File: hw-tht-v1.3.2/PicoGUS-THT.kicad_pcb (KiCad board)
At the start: 2 copper layers, 103.7 x 99.8 mm, 88 parts, among them J1 IRQDMA_JP, J11 USB-A, J3 Bus_ISA_8bit, J5 SJ1-3535NG, J6 UART_TX, J7 USB power jumper, J8 SJ1-3535NG-GR, J9 Waveblaster, U1 Pico, U10 74AHCT126, U11 NE5532, U12 USBLC6-2SC6, U2 74AHC244, U3 SN74CB3T3257, U4 SN74CB3T3257, U5 74AHC14, U6 74AHC00, U7 74AHC00, U8 APS6404L-3SQR-SN, U9 PCM5100A

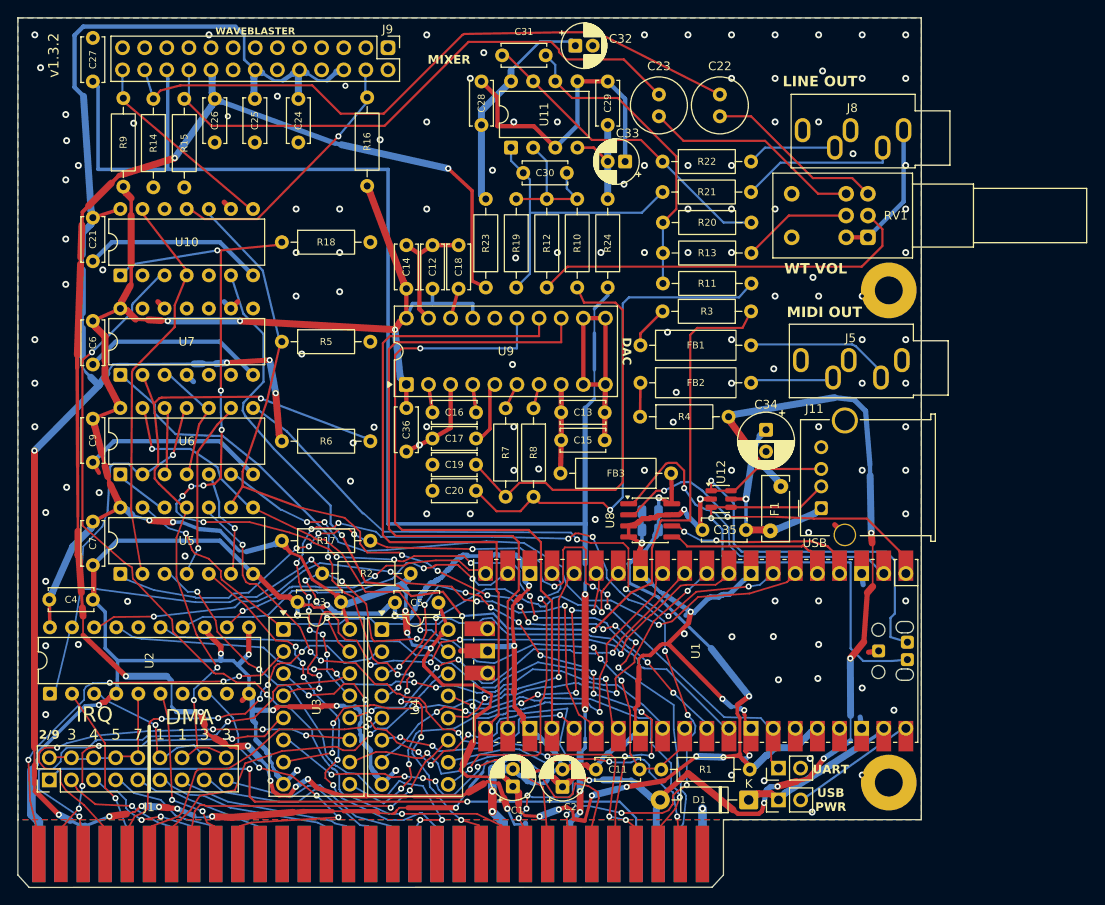
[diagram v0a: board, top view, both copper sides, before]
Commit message: THT v1.3.2: adopt the 102 mm placement (unrouted) with 3D models
The board now holds the new hand placement on a 102.0 mm outline in place
of the routed 103.7 mm layout (that one stays in 8dbb6c6). It has no
tracks or vias yet and has to be routed again.

- Logic column in line with U2 with the decoupling discs between the
  chips, R18/R5/R6/R17 vertical, DAC group 15 mm left, FB3 vertical,
  copper logo along the top edge over LINE OUT, several labels moved.
- C8/C10 back to the v1.3.1 Murata through-hole discs, in a row above
  U8 (schematic fields, BOM and DigiKey upload files updated).
- Back princess artwork removed (to be UV printed); back texts kept.
- Bracket end trimmed 1.84 mm (JLCPCB prices <= 102 mm lower). H1/H2
  1.70 mm, J8 1.10, J5 0.90, Pico 1.35 (with its slots and rule areas),
  U4 0.45 and U3 0.35 mm moved so copper stays >= 0.35 mm from the edge.
  The bracket tab holes are now 7.03 mm behind the plate: it needs a
  bracket with longer tabs (3D-printed).
- U1 uses the new RPi_Pico_SMD_TH_USB_NoSWD footprint (no SMD pads for
  the unconnected SWD castellations, tighter courtyard).
- 3D models for every part: CUI jacks (J5 a black copy of the CUI
  model), Alps RK09712 pot, a generated MF-R050 model, U3/U4/U9 socket +
  adapter stacks exported from the adapter PCBs, KiCad's Pico model,
  J9's model path fixed. Library footprints carry the same models.
- Schematic title note and PDF updated; README rewritten for the
  adopted, unrouted layout.

DRC with schematic parity: 12 accepted courtyard overlaps in the logic
column, 309 unconnected (unrouted), warnings only otherwise; ERC as before.

Co-Authored-By: Claude Opus 5.5 <noreply@anthropic.com>
Claude-Session: https://claude.ai/code/session_011utN3x8yYUNDvkpGCEq5yD
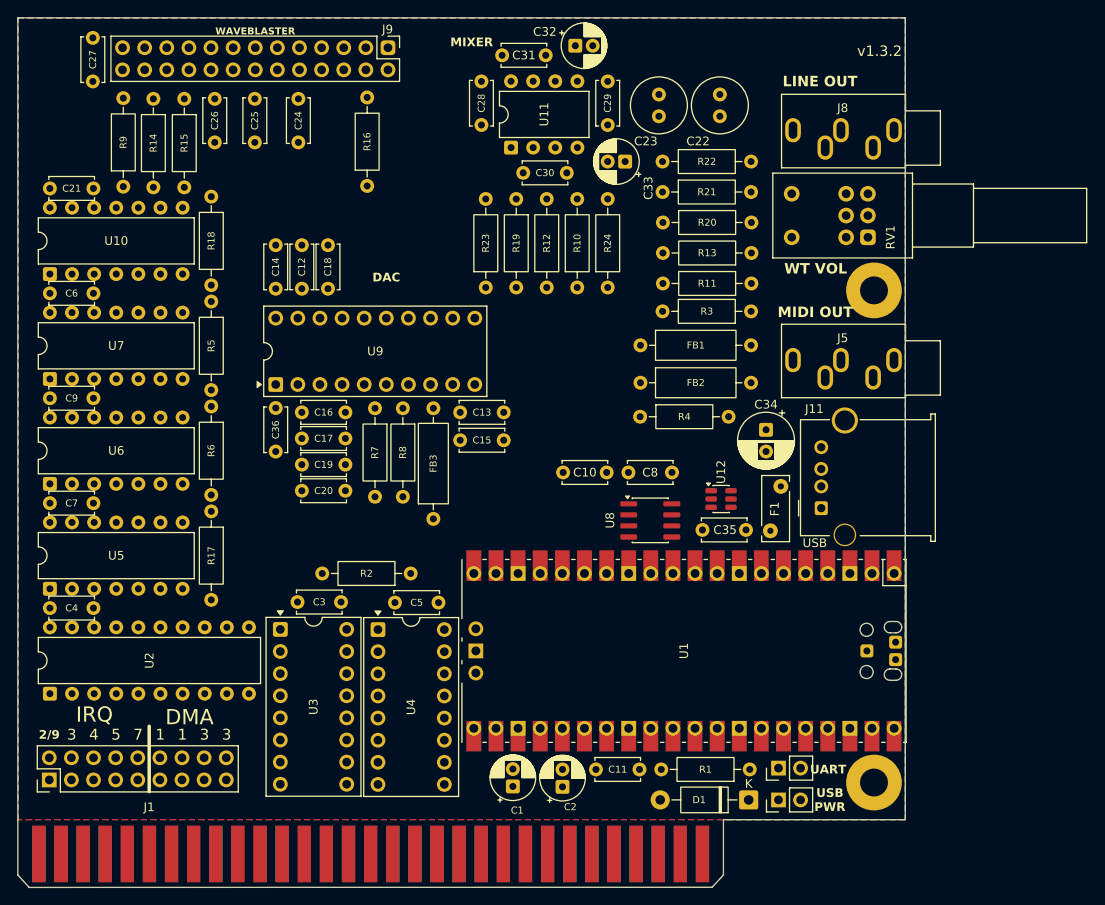
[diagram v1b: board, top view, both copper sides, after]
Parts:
- C10, C8: footprint Capacitor_SMD:C_0805_2012Metric -> Capacitor_THT:C_Disc_D5.0mm_W2.5mm_P5.00mm; moved to F.Cu
- U1: footprint PiGUS library:RPi_Pico_SMD_TH_USB -> PiGUS library:RPi_Pico_SMD_TH_USB_NoSWD
- moved FB3 27.8 mm to (164.1, 93.7), turned to 90 degrees
- moved C12 15.0 mm to (149.0, 62.3)
- moved C14 15.0 mm to (146.0, 62.3)
- moved C16 15.0 mm to (149.0, 81.5)
- moved C17 15.0 mm to (154.0, 84.5)
- moved C18 15.0 mm to (152.0, 67.3)
- moved C19 15.0 mm to (149.0, 87.5)
- moved C20 15.0 mm to (149.0, 90.5)
- moved C36 15.0 mm to (146.0, 81.0)
- moved R7 15.0 mm to (157.4, 81.0)
- moved R8 15.0 mm to (160.6, 81.0)
- moved U9 15.0 mm to (146.0, 78.3)
- moved C13 11.6 mm to (172.2, 81.5)
- moved C15 11.6 mm to (167.2, 84.7)
- moved R18 9.65 mm to (138.6, 56.7), turned to -90 degrees
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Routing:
- net GND: track 501.6 -> 0.00 mm, vias 145 -> 0
- net +5V: track 352.1 -> 0.00 mm, vias 19 -> 0
- net +3V3: track 305.9 -> 0.00 mm, vias 16 -> 0
- net +12V: track 186.9 -> 0.00 mm, vias 9 -> 0
- net -12V: track 185.3 -> 0.00 mm, vias 4 -> 0
- net ~{RI/OCHRDY}: track 125.3 -> 0.00 mm, vias 14 -> 0
- net Net-(R3-Pad1): track 120.5 -> 0.00 mm, vias 3 -> 0
- net RESET: track 118.7 -> 0.00 mm, vias 9 -> 0
- net D2: track 109.5 -> 0.00 mm, vias 15 -> 0
- net ~{BUSOE}: track 103.6 -> 0.00 mm, vias 7 -> 0
- net UART_TX: track 101.9 -> 0.00 mm, vias 9 -> 0
- net I/OCHRDY: track 101.0 -> 0.00 mm, vias 3 -> 0
- net RUN: track 90.7 -> 0.00 mm, vias 5 -> 0
- net BCK: track 81.0 -> 0.00 mm
- net ADS: track 80.3 -> 0.00 mm, vias 1 -> 0
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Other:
- board size 103.7 x 99.8 mm -> 101.9 x 99.8 mm
